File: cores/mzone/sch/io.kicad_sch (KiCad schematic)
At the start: 41 parts

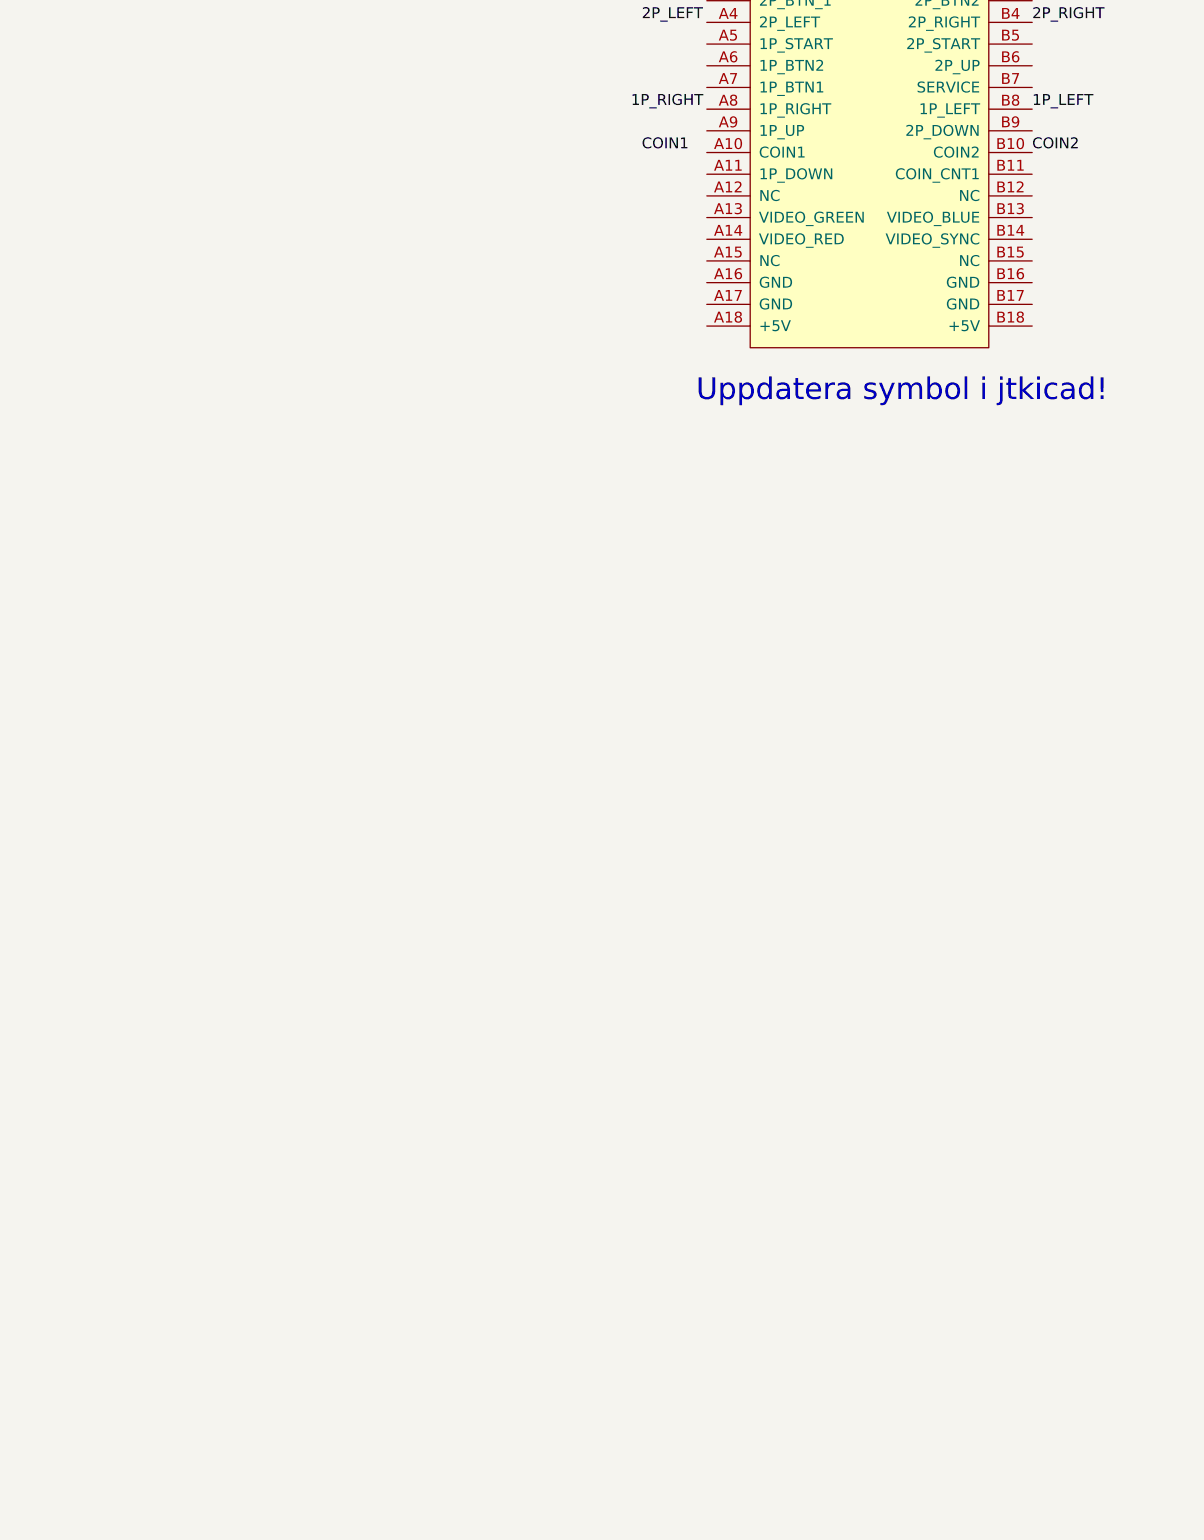
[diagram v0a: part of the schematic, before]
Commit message: mzone core
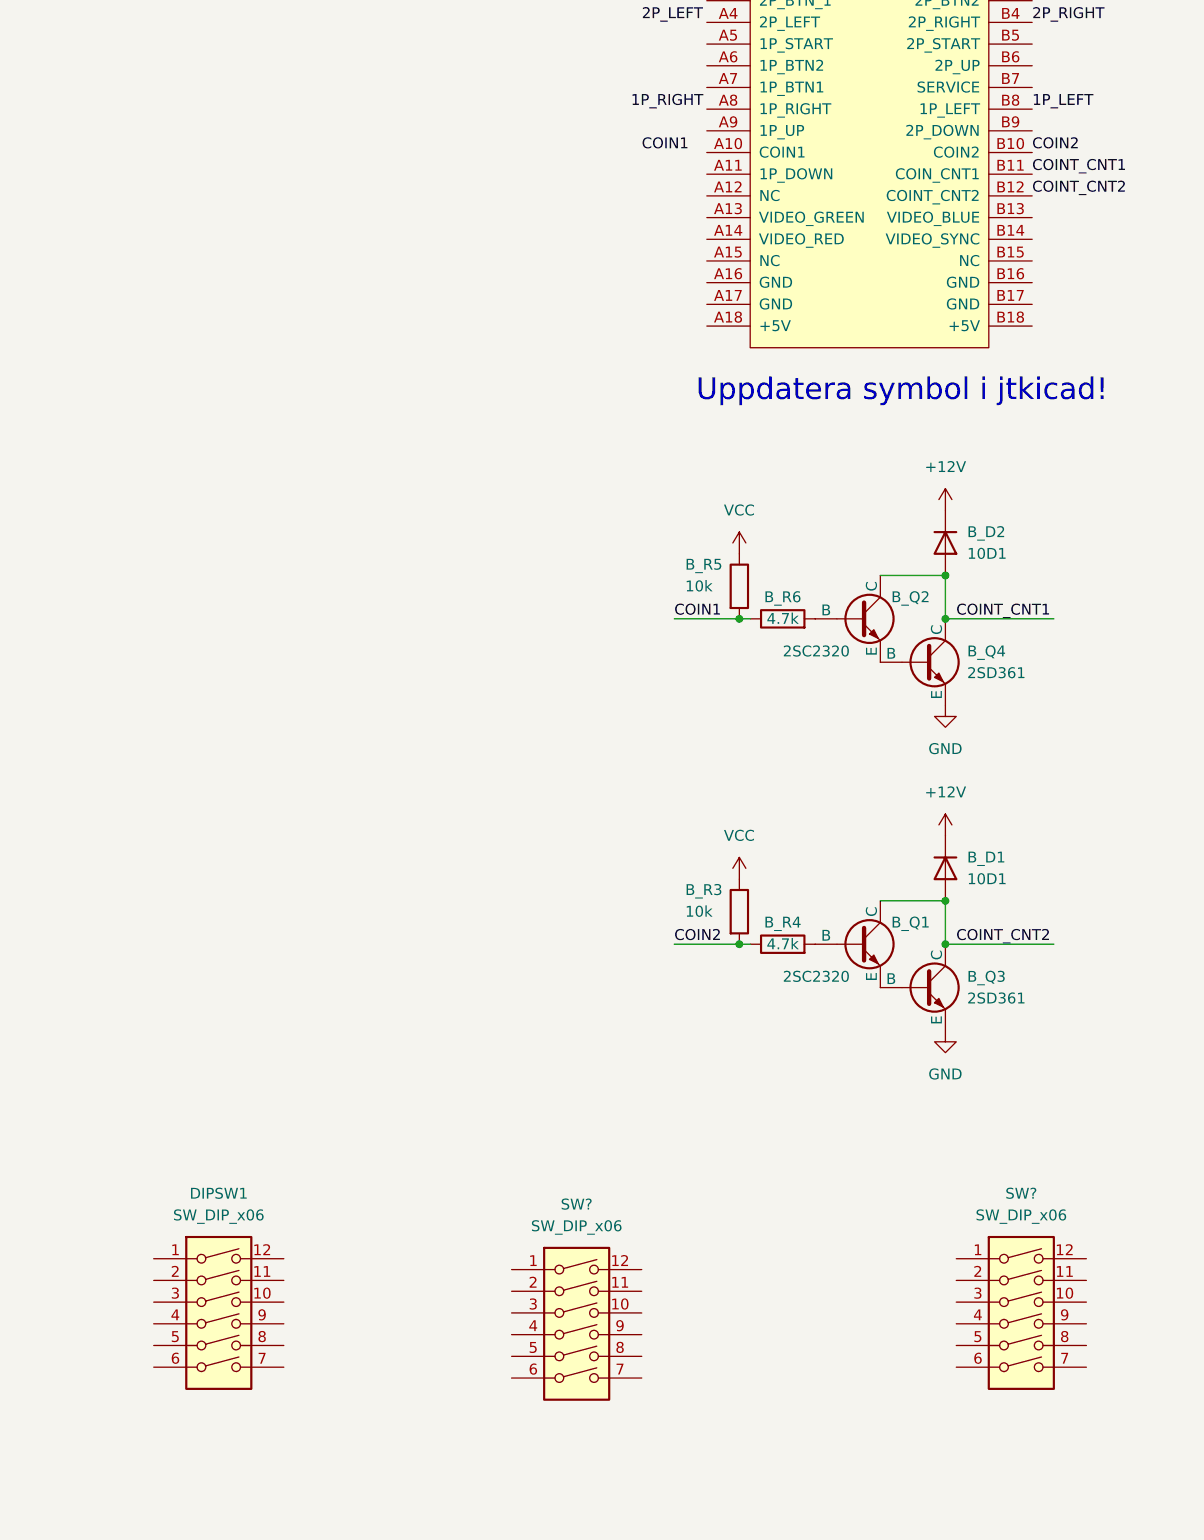
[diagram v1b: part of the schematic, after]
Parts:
- added B_D1, B_D2: 10D1, symbol Device:D
- added B_Q1, B_Q2: 2SC2320, symbol Simulation_SPICE:NPN
- added B_Q3, B_Q4: 2SD361, symbol Simulation_SPICE:NPN
- added B_R3, B_R5: 10k, symbol Device:R
- added B_R4, B_R6: 4.7k, symbol Device:R
- added DIPSW1, SW? (x2): SW_DIP_x06, symbol Switch:SW_DIP_x06
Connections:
- net COIN1: now also B_R5.2, B_R6.1
- net COIN2: now also B_R3.2, B_R4.1
- net GND: now also B_Q3.3 (E), B_Q4.3 (E)
- net VCC: now also B_R3.1, B_R5.1
- net COINT_CNT1: now reaches U?.B11 (COIN_CNT1)
- net COINT_CNT1: now also B_D2.2 (A), B_Q2.1 (C), B_Q4.1 (C)
- net COINT_CNT2: now reaches U?.B12 (COINT_CNT2)
- net COINT_CNT2: now also B_D1.2 (A), B_Q1.1 (C), B_Q3.1 (C)
- new net: B_Q1.3 (E), B_Q3.2 (B)
- new net: B_Q2.2 (B), B_R6.2
- new net: B_Q2.3 (E), B_Q4.2 (B)
- new net: B_Q1.2 (B), B_R4.2
- new net +12V: B_D1.1 (K), B_D2.1 (K)

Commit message: mzone core
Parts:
- removed DIPSW1, SW? (x2): SW_DIP_x06, symbol Switch:SW_DIP_x06
- added unit 4 of B_C13
- added unit 3 of B_C13
- added B_C36, B_C37: 47u, symbol Device:C_Polarized
- added B_C38: 10n, symbol Device:C
- added B_C39: 220u, symbol Device:C_Polarized
- added B_C41: 47n, symbol Device:C
- added B_D14: 74LS240, symbol 74xx:74LS240_Split
- added B_D15: 555, Package_DIP:DIP-8_W7.62mm, symbol Timer:ICM7555xP
- added B_D3: 1S1588, symbol Device:D
- added B_D4: 10D1, symbol Device:D
- added B_DE11: 74LS02, symbol jt74:74LS02
- added B_DE13: 74LS00, symbol jt74:74LS00
- added B_E14, B_E15: 74LS293, symbol skutis:74LS293
- added B_G1, B_G2: 74LS257, symbol jt74:74LS257
- added B_J1: SolderJumper_2_Open, symbol Jumper:SolderJumper_2_Open
- added B_Q5: 2SC2320, symbol Simulation_SPICE:NPN
- added B_Q6: 2SA697, symbol Simulation_SPICE:PNP
- added B_R54: 4k7, symbol Device:R
- added B_R55: 4.7k, symbol Device:R
- added B_R65, B_R69: 10k, symbol Device:R
- added B_R66: 1k, symbol Device:R
- added B_R68: 20k, symbol Device:R
- added DSW1, DSW2: SW_DIP_x08, symbol Switch:SW_DIP_x08
- added R67: 470R, symbol Device:R
- added RA1, RA2: 4k7 x 8, Resistor_THT:R_Array_SIP9, symbol Device:R_Network08
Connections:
- net AS0: now also B_G1.1 (S), B_G2.1 (S)
- net DB0: now also B_G2.4 (Za)
- net DB1: now also B_G2.7 (Zb)
- net DB2: now also B_G2.9 (Zc)
- net DB3: now also B_G2.12 (Zd)
- net DB4: now also B_G1.4 (Za)
- net DB5: now also B_G1.7 (Zb)
- net GND: now also B_C36.2, B_C37.2, B_C38.2, B_C39.2, B_C41.2, B_D15.1 (GND), B_G1.8 (GND), B_G2.8 (GND), B_J1.1 (A), B_Q5.3 (E), B_R68.2, DSW1.10, DSW1.11, DSW1.12, DSW1.13, DSW1.14, DSW1.15, DSW1.16, DSW1.9, DSW2.10, DSW2.11, DSW2.12, DSW2.13, DSW2.14, DSW2.15, DSW2.16, DSW2.9
- net VCC: now also B_D15.4 (R), B_D15.8 (VCC), B_D3.1 (K), B_D4.2 (A), B_G1.16 (VCC), B_G2.16 (VCC), B_R54.1, B_R55.1, B_R65.1, B_R69.1, R67.1, RA1.1 (common), RA2.1 (common)
- new net: B_Q6.1 (C), B_R66.1
- new net: B_Q5.2 (B), B_R66.2, B_R68.1
- new net: B_C13.13, B_C36.1, B_D15.2 (TR), B_D3.2 (A), B_Q5.1 (C), B_R69.2
- new net: B_DE13.10, B_DE13.12, B_J1.2 (B), B_R55.2
- new net: B_C13.10, B_C13.11
- new net: B_C13.12, B_D14.3
- new net: B_Q6.2 (B), R67.2
- new net: B_C39.1, B_D4.1 (K), B_Q6.3 (E)
- new net: B_DE13.8, B_E15.12 (R01), B_E15.13 (R02)
- new net: B_C38.1, B_D15.5 (CV)
- new net: B_D14.17, B_D15.3 (Q)
- new net: B_C37.1, B_D15.6 (THR), B_D15.7 (DIS), B_R65.2
- new net: B_C13.9, B_DE11.10
- new net: B_DE13.11, B_E14.12 (R01), B_E14.13 (R02)
- new net: B_E14.11 (CKB), B_E14.9 (Q0)
- new net: B_DE11.8, B_E14.8 (Q3)
- new net: B_DE11.9, B_E15.8 (Q3)
- new net: B_E15.11 (CKB), B_E15.9 (Q0)
- new net DB6: B_G1.9 (Zc)
- new net DB7: B_G1.12 (Zd)
- new net DSW10: B_G2.3 (I1a), DSW1.1, RA1.9 (R8)
- new net DSW11: B_G2.6 (I1b), DSW1.2, RA1.8 (R7)
- new net DSW12: B_G2.10 (I1c), DSW1.3, RA1.7 (R6)
- new net DSW13: B_G2.13 (I1d), DSW1.4, RA1.6 (R5)
- new net DSW14: B_G1.3 (I1a), DSW1.5, RA1.5 (R4)
- new net DSW15: B_G1.6 (I1b), DSW1.6, RA1.4 (R3)
- new net DSW16: B_G1.10 (I1c), DSW1.7, RA1.3 (R2)
- new net DSW17: B_G1.13 (I1d), DSW1.8, RA1.2 (R1)
- new net DSW20: B_G2.2 (I0a), DSW2.1, RA2.9 (R8)
- new net DSW21: B_G2.5 (I0b), DSW2.2, RA2.8 (R7)
- new net DSW22: B_G2.11 (I0c), DSW2.3, RA2.7 (R6)
- new net DSW23: B_G2.14 (I0d), DSW2.4, RA2.6 (R5)
- new net DSW24: B_G1.2 (I0a), DSW2.5, RA2.5 (R4)
- new net DSW25: B_G1.5 (I0b), DSW2.6, RA2.4 (R3)
- new net DSW26: B_G1.11 (I0c), DSW2.7, RA2.3 (R2)
- new net DSW27: B_G1.14 (I0d), DSW2.8, RA2.2 (R1)
- new net ~{AFR1}: B_DE13.9
- new net ~{AFR2}: B_DE13.13
- new net ~{DIP}: B_G1.15 (OE), B_G2.15 (OE)
- new net ~{RESET}: B_C13.8, B_C41.1, B_R54.2
- new net ~{VBLANK}: B_E14.10 (CKA), B_E15.10 (CKA)
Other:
- note added: "Coin counters"
- note added: "Watchdog and reset"
- moved on the sheet: B_C11, B_C12, B_C13, B_C14, B_C15, B_C16, B_C17, B_C18, B_C19, B_C20, B_C21, B_C22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

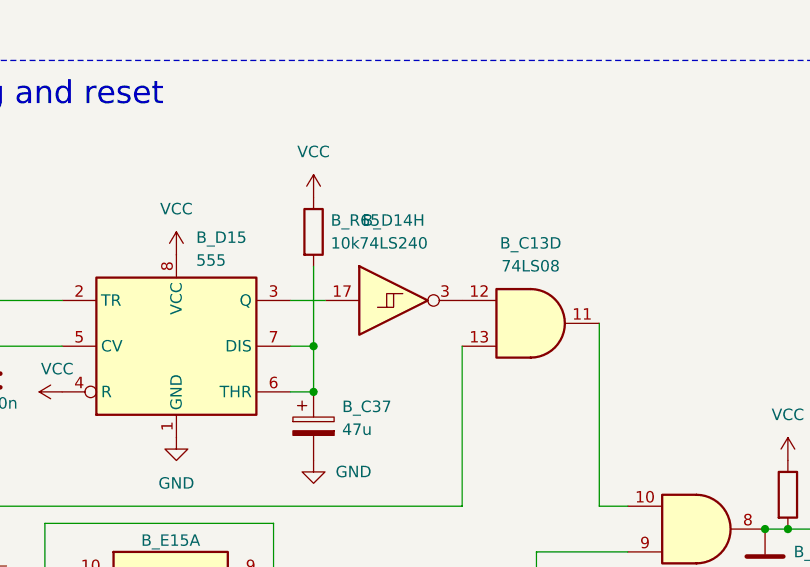
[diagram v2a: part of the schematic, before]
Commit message: mzone core
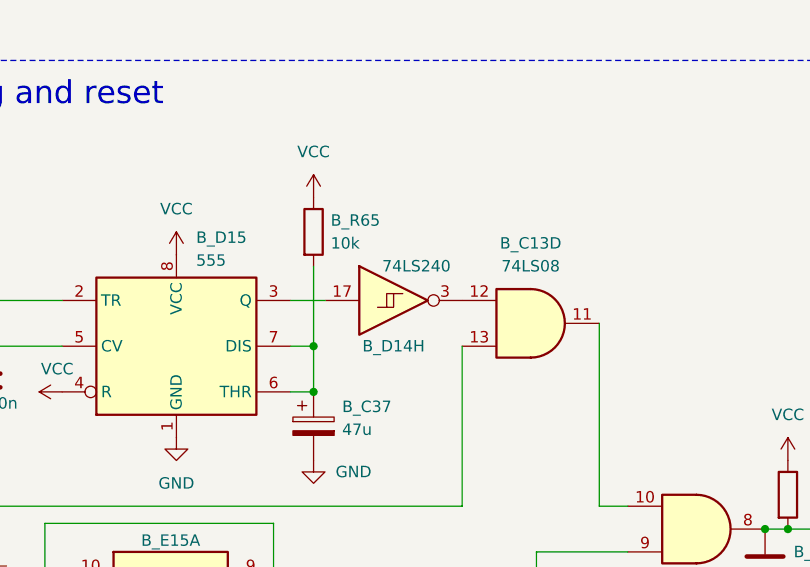
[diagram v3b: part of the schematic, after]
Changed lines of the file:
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@@
 		(on_board yes)
 		(dnp no)
-		(fields_autoplaced yes)
 		(property "Reference" "B_D14"
-			(at 345.44 173.99 0)
+			(at 345.44 187.96 0)
 			(effects
 				(font
@@
 		)
 		(property "Value" "74LS240"
-			(at 345.44 176.53 0)
+			(at 347.98 179.07 0)
 			(effects
 				(font

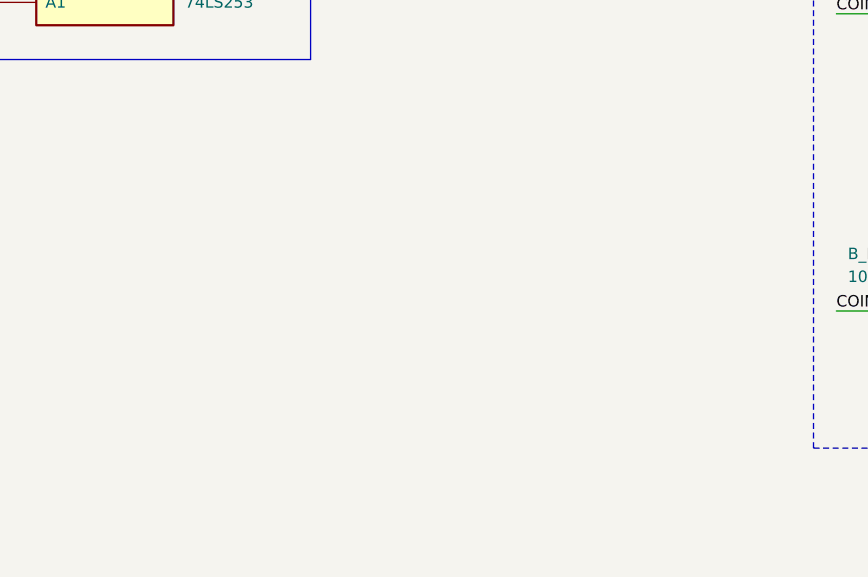
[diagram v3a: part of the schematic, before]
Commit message: mzone core
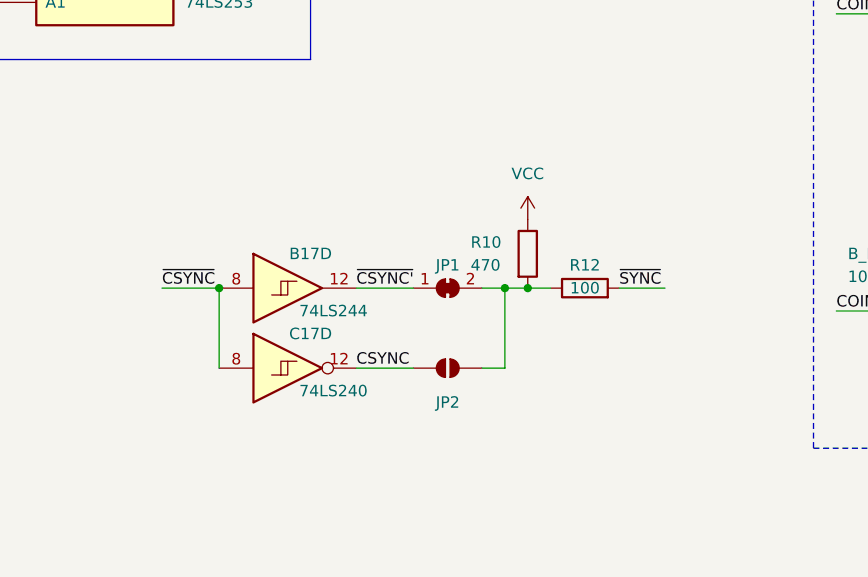
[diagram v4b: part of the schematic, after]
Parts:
- added B17: 74LS244, symbol 74xx:74LS244_Split
- added C17: 74LS240, symbol 74xx:74LS240_Split
- added JP1: SolderJumper_2_Bridged, symbol Jumper:SolderJumper_2_Bridged
- added JP2: SolderJumper_2_Open, symbol Jumper:SolderJumper_2_Open
- added R10: 470, symbol Device:R
- added R12: 100, symbol Device:R
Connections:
- net VCC: now also R10.1
- new net: JP1.2 (B), JP2.2 (B), R10.2, R12.1
- new net CSYNC: C17.12, JP2.1 (A)
- new net ~{CSYNC'}: B17.12, JP1.1 (A)
- new net ~{CSYNC}: B17.8, C17.8
- new net ~{SYNC}: R12.2

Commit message: mzone core
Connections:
- net COIN1: no longer B_R5.2, B_R6.1
- net COIN2: no longer B_R3.2, B_R4.1
- net GND: now also B_E14.7 (GND), B_E15.7 (GND)
- net VCC: now also B_E14.14 (VCC), B_E15.14 (VCC)
- new net COIN_CNT'_1: B_R5.2, B_R6.1
- new net COIN_CNT'_2: B_R3.2, B_R4.1
- no-connect marks 0 -> 6
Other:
- moved on the sheet: B_E14B, B_E15B

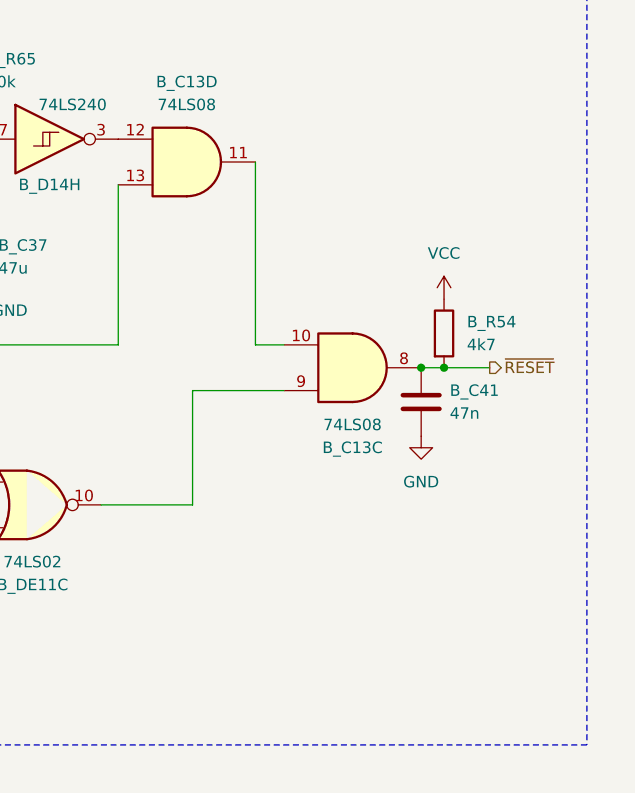
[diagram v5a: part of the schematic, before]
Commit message: mzone core
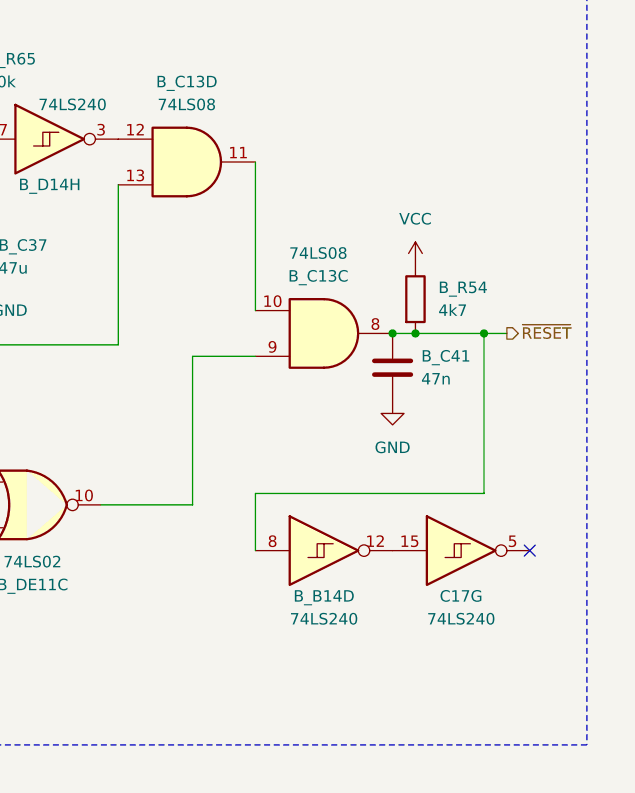
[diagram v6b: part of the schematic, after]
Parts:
- added B_B14: 74LS240, symbol 74xx:74LS240_Split
- added unit 7 of C17
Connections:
- net ~{RESET}: now also B_B14.8
- new net: B_B14.12, C17.15
- no-connect marks 6 -> 7
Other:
- moved on the sheet: B_C13C, B_C41, B_R54
